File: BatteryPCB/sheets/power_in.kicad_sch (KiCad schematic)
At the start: 8 parts, among them SW1 CAM POWER

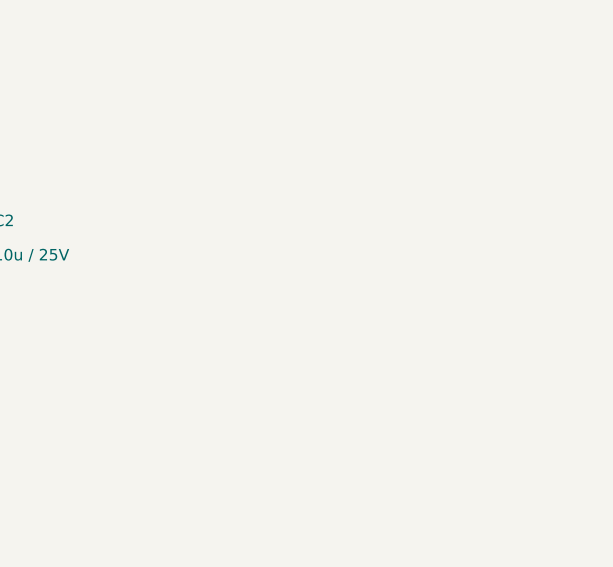
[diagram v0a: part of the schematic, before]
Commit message: Battery PCB v17: test points, strict design rules, review fixes
- Test points: TP1 +5V (buck output), TP2 VBAT+ (2S pack), TP3/TP4 GND;
  2 mm through-hole pads placed where both sides are open
- Strict rules in the project: 0.25/0.3/0.4 mm clearance (signal/power/pyro),
  0.3 mm hole clearance, 0.5 mm hole-to-hole, 0.15 mm via ring, silk spacing;
  every DRC check is an error. Fixed the spots they flagged around U1, R4, C8,
  D1/D3 silk and the TP4 label
- R5 47k -> 39k so VBAT_SENSE stays inside the ESP32 ADC range at a full pack
- BOM note: the RunCam needs a built harness (3-pin power/video + RX/TX pads)
- README: exact ESP32 to buy (ESP32-DevKitC-32E, not WROVER or 30-pin clones),
  design rules, sense scaling; layout notes for v17
- Checks: ERC 0 errors; DRC 0 violations incl. warnings with schematic parity;
  all 115 schematic pins match board pad nets; verify_A ALL PASS

Co-Authored-By: Claude Opus 5.5 <noreply@anthropic.com>
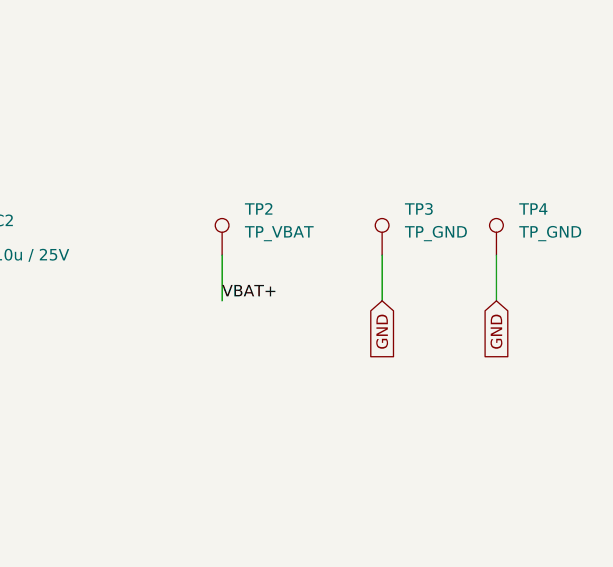
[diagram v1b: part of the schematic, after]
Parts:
- added TP2: TP_VBAT, TestPoint:TestPoint_THTPad_D2.0mm_Drill1.0mm, symbol Connector:TestPoint
- added TP3, TP4: TP_GND, TestPoint:TestPoint_THTPad_D2.0mm_Drill1.0mm, symbol Connector:TestPoint
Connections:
- net GND: now also TP3.1, TP4.1
- net VBAT+: now also TP2.1
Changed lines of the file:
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@@
 		(effects (font (size 1.8 1.8) (bold yes)) (justify left bottom))
 	)
+	(symbol
+		(lib_id "Connector:TestPoint")
+		(at 233.68 45.72 0)
+		(unit 1)
+		(exclude_from_sim no)
+		(in_bom no)
+		(on_board yes)
+		(dnp no)
+		(property "Reference" "TP2"
+			(at 236.22 40.64 0)
+			(effects (font (size 1.27 1.27)) (justify left))
+		)
+		(property "Value" "TP_VBAT"
+			(at 236.22 43.18 0)
+			(effects (font (size 1.27 1.27)) (justify left))
+		)
+		(property "Footprint" "TestPoint:TestPoint_THTPad_D2.0mm_Drill1.0mm"
+			(at 233.68 45.72 0)
+			(effects (font (size 1.27 1.27)) (hide yes))
+		)
+		(property "Datasheet" "~"
+			(at 233.68 45.72 0)
+			(effects (font (size 1.27 1.27)) (hide yes))
+		)
+		(property "Description" "Bench test point"
+			(at 233.68 45.72 0)
+			(effects (font (size 1.27 1.27)) (hide yes))
+		)
+		(pin "1")
+		(instances
+			(project "battery_pcb"
+				(path "/19ef3a32-de7c-46ee-a850-2420f6d47f94/ae01c8e7-4191-4202-a535-afc32959794b"
+					(reference "TP2")
+					(unit 1)
+				)
+			)
+		)
+	)
+	(wire
+		(pts (xy 233.68 45.72) (xy 233.68 50.80))
+		(stroke (width 0) (type default))
+	)
+	(label "VBAT+"
+		(at 233.68 50.80 0)
+		(fields_autoplaced yes)
+		(effects (font (size 1.27 1.27)) (justify left bottom))
+	)
+	(symbol
+		(lib_id "Connector:TestPoint")
+		(at 251.46 45.72 0)
+		(unit 1)
+		(exclude_from_sim no)
+		(in_bom no)
+		(on_board yes)
+		(dnp no)
+		(property "Reference" "TP3"
+			(at 254.00 40.64 0)
+			(effects (font (size 1.27 1.27)) (justify left))
+		)
+		(property "Value" "TP_GND"
+			(at 254.00 43.18 0)
+			(effects (font (size 1.27 1.27)) (justify left))
+		)
+		(property "Footprint" "TestPoint:TestPoint_THTPad_D2.0mm_Drill1.0mm"
+			(at 251.46 45.72 0)
+			(effects (font (size 1.27 1.27)) (hide yes))
+		)
+		(property "Datasheet" "~"
+			(at 251.46 45.72 0)
+			(effects (font (size 1.27 1.27)) (hide yes))
+		)
+		(property "Description" "Bench test point"
+			(at 251.46 45.72 0)
+			(effects (font (size 1.27 1.27)) (hide yes))
+		)
+		(pin "1")
+		(instances
+			(project "battery_pcb"
+				(path "/19ef3a32-de7c-46ee-a850-2420f6d47f94/ae01c8e7-4191-4202-a535-afc32959794b"
+					(reference "TP3")
+					(unit 1)
+				)
+			)
+		)
+	)
+	(wire
+		(pts (xy 251.46 45.72) (xy 251.46 50.80))
+		(stroke (width 0) (type default))
+	)
+	(global_label "GND"
+		(shape input)
+		(at 251.46 50.80 270)
+		(fields_autoplaced yes)
+		(effects (font (size 1.27 1.27)) (justify right))
+		(property "Intersheetrefs" "${INTERSHEET_REFS}"
+			(at 251.46 55.80 0)
+			(effects (font (size 1.27 1.27)) (hide yes))
+		)
+	)
+	(symbol
+		(lib_id "Connector:TestPoint")
+		(at 264.16 45.72 0)
+		(unit 1)
+		(exclude_from_sim no)
+		(in_bom no)
+		(on_board yes)
+		(dnp no)
+		(property "Reference" "TP4"
+			(at 266.70 40.64 0)
+			(effects (font (size 1.27 1.27)) (justify left))
+		)
+		(property "Value" "TP_GND"
+			(at 266.70 43.18 0)
+			(effects (font (size 1.27 1.27)) (justify left))
+		)
+		(property "Footprint" "TestPoint:TestPoint_THTPad_D2.0mm_Drill1.0mm"
+			(at 264.16 45.72 0)
+			(effects (font (size 1.27 1.27)) (hide yes))
+		)
+		(property "Datasheet" "~"
+			(at 264.16 45.72 0)
+			(effects (font (size 1.27 1.27)) (hide yes))
+		)
+		(property "Description" "Bench test point"
+			(at 264.16 45.72 0)
+			(effects (font (size 1.27 1.27)) (hide yes))
+		)
+		(pin "1")
+		(instances
+			(project "battery_pcb"
+				(path "/19ef3a32-de7c-46ee-a850-2420f6d47f94/ae01c8e7-4191-4202-a535-afc32959794b"
+					(reference "TP4")
+					(unit 1)
+				)
+			)
+		)
+	)
+	(wire
+		(pts (xy 264.16 45.72) (xy 264.16 50.80))
+		(stroke (width 0) (type default))
+	)
+	(global_label "GND"
+		(shape input)
+		(at 264.16 50.80 270)
+		(fields_autoplaced yes)
+		(effects (font (size 1.27 1.27)) (justify right))
+		(property "Intersheetrefs" "${INTERSHEET_REFS}"
+			(at 264.16 55.80 0)
+			(effects (font (size 1.27 1.27)) (hide yes))
+		)
+	)
 )

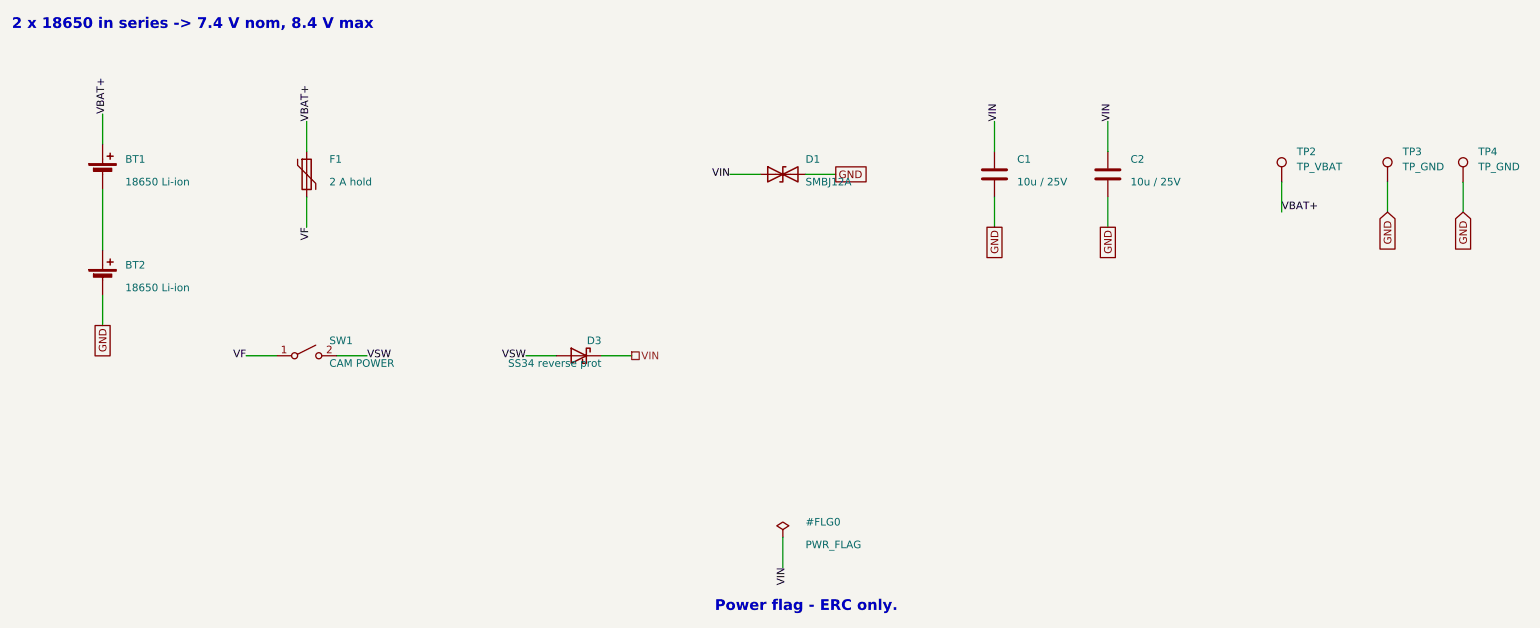
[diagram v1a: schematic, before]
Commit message: Battery PCB v19: UVLO on the buck, input caps, 6.8 uH, wired schematic
Third review (design check of the power path):
- U1 EN gets an R9/R10 divider (UVLO: on 6.3 V, off 5.5 V at VIN) so
  the 2S pack is no longer run down to 1.8 V per cell.
- Input caps per the LMR51430 datasheet: C1 is the 100 nF at U1's pins,
  C2 + new C11 (10 uF) are the bulk.
- L1 6.8 uH (TI's value for 500 kHz / 5 V out), same footprint.
- Sheets 1-3 redrawn with wires; C1/C2 moved next to U1; stale 47k
  divider note and the SS34 value on D3 corrected.
ERC 0 errors, DRC 0 (strict, schematic parity), verify_A all pass.

Co-Authored-By: Claude Opus 5.5 <noreply@anthropic.com>
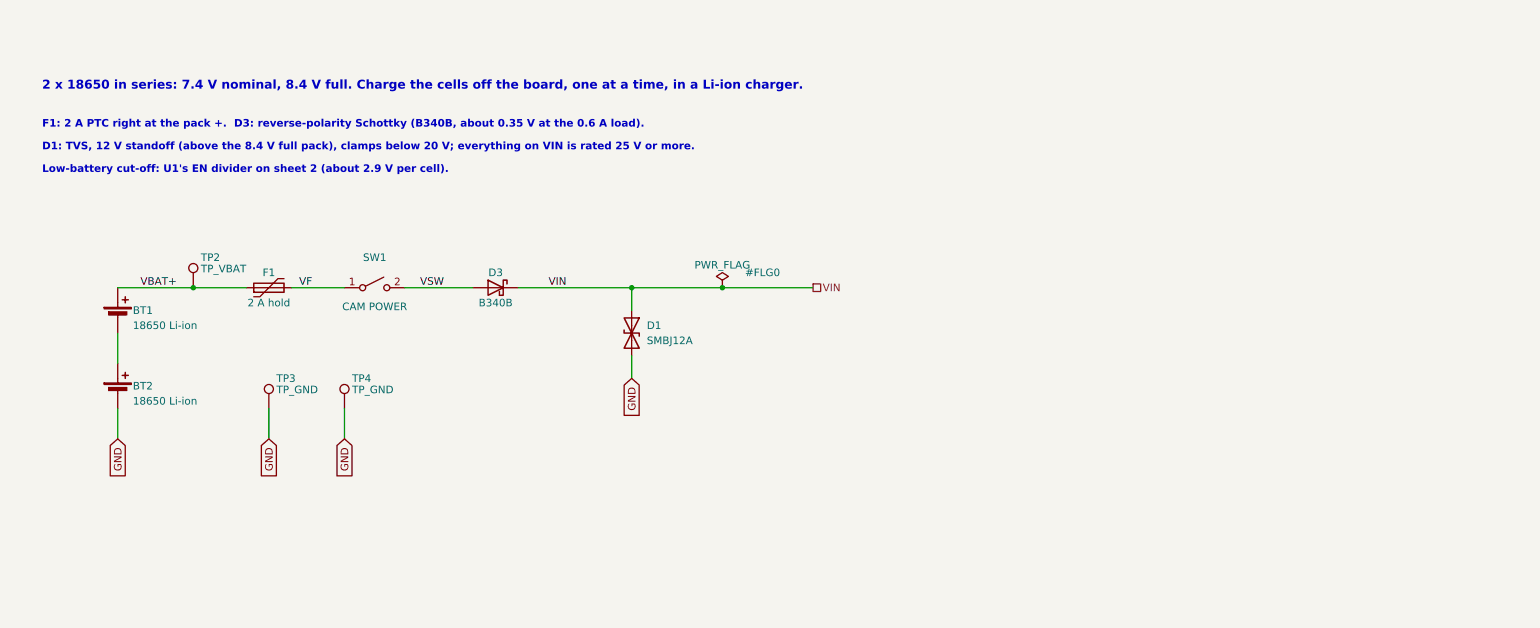
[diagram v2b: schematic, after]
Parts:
- removed C1, C2: 10u / 25V, Capacitor_SMD:C_0805_2012Metric, symbol Device:C
- D3: value SS34 reverse prot -> B340B
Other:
- note added: "2 x 18650 in series: 7.4 V nominal, 8.4 V full. Charge the cells off the board, one at a time, in a Li-ion charger."
- note added: "D1: TVS, 12 V standoff (above the 8.4 V full pack), clamps below 20 V; everything on VIN is rated 25 V or more."
- note added: "F1: 2 A PTC right at the pack +. D3: reverse-polarity Schottky (B340B, about 0.35 V at the 0.6 A load)."
- note added: "Low-battery cut-off: U1's EN divider on sheet 2 (about 2.9 V per cell)."
- note removed: "2 x 18650 in series -> 7.4 V nom, 8.4 V max"
- note removed: "Power flag - ERC only."
- moved on the sheet: BT1, BT2, D1, D3, F1, SW1, TP2, TP3, TP4
